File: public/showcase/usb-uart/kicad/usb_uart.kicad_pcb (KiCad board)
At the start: 4 copper layers, 45 x 35.7 mm, 32 parts, among them J1 TYPE-C-31-M-12, J2 UART1, J3 FLOW1, J4 RS485, U1 CH342F, U2 LDO, U3 THVD1450D

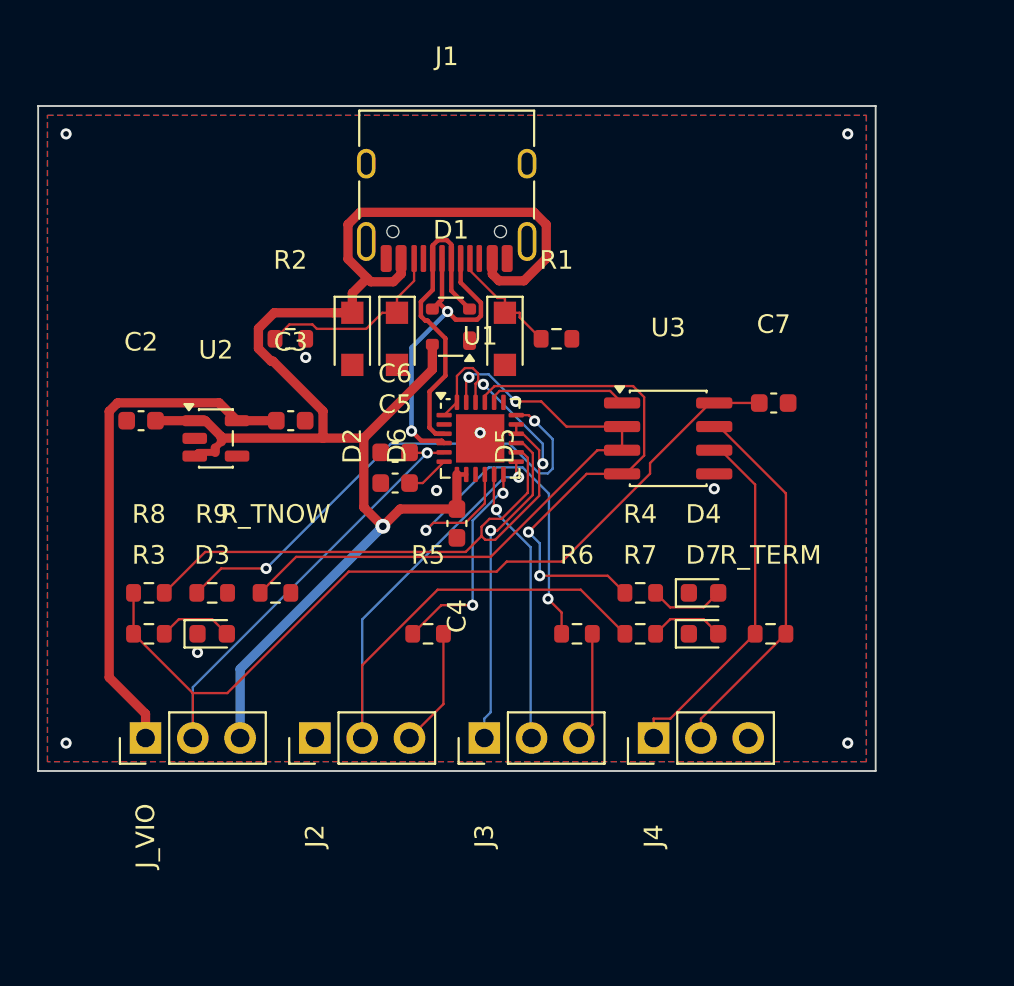
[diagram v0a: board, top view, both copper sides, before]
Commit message: NOISSUE - Update the showcase to board revision B and state its qualification status
Addresses the review on #5: the published route record no longer says fabrication_ready (it is false), the page is labelled an engineering draft with the qualification matrix, gate result and file hashes, every artifact names one revision, and the protection claim says the RS-485 network is not surge-tested.

Signed-off-by: nyagamunene <stevenyaga2014@gmail.com>
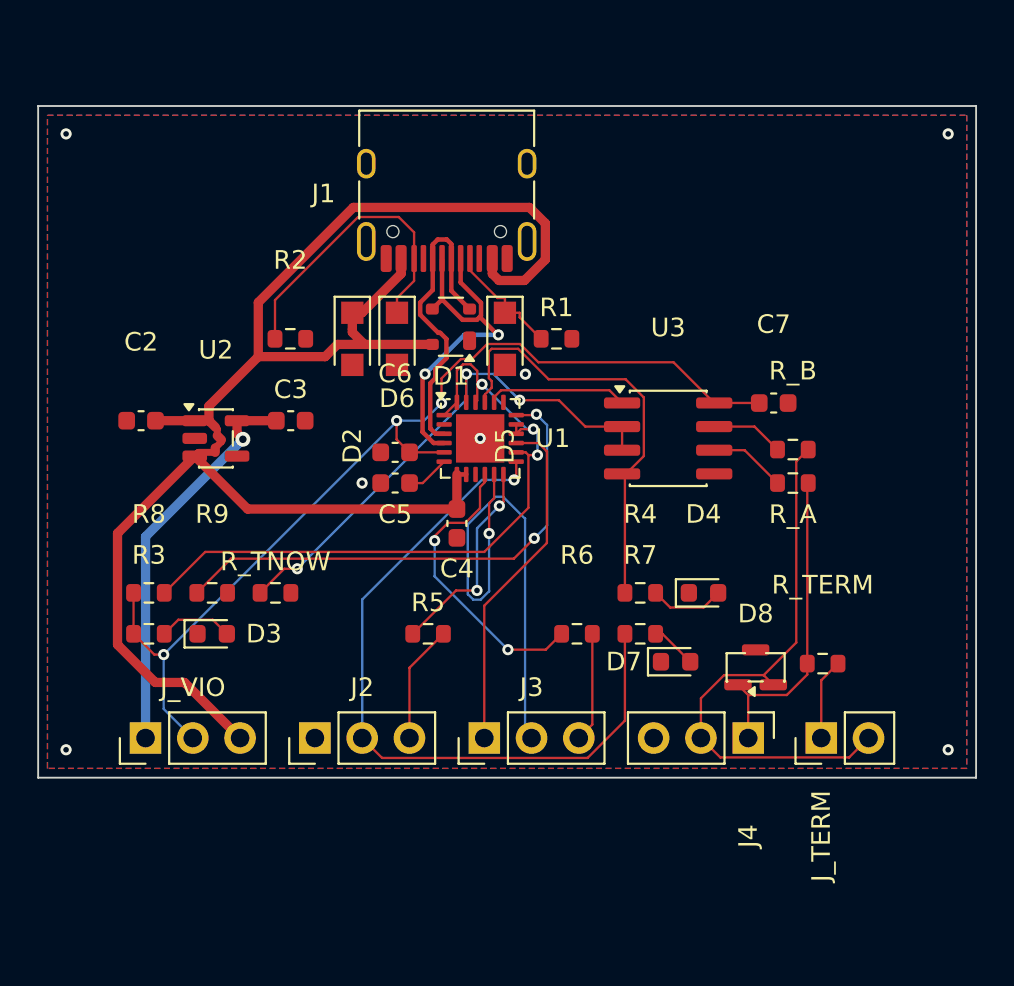
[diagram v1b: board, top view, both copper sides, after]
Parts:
- added D8: TVS, Package_TO_SOT_SMD:SOT-23, F.Cu at (38.6, 29.6)
- added J_TERM: TERM, Connector_PinHeader_2.54mm:PinHeader_1x02_P2.54mm_Vertical, F.Cu at (42.1, 33.4)
- added R_A: 10ohm, Resistor_SMD:R_0603_1608Metric, F.Cu at (40.6, 19.7)
- added R_B: 10ohm, Resistor_SMD:R_0603_1608Metric, F.Cu at (40.6, 17.9)
- moved J4 5.08 mm to (38.2, 33.4), turned to 270 degrees
- moved R_TERM 3.22 mm to (42.2, 29.4)
- moved D7 2.12 mm to (34.3, 29.3)
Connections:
- J4 pad 1: RS485_A -> RS485_A_BUS
- J4 pad 2: RS485_B -> RS485_B_BUS
- R_TERM pad 1: RS485_A -> RS485_A_BUS
- R_TERM pad 2: RS485_B -> RS485_TERM
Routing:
- net RS485_B_BUS: track 0.00 -> 29.7 mm
- net RS485_A_BUS: track 0.00 -> 17.0 mm
- net RS485_B: track 20.4 -> 3.91 mm
- net RS485_A: track 19.4 -> 4.13 mm
- net VIO: track 68.8 -> 54.3 mm, vias 1 -> 3
- net RTS1: track 15.0 -> 27.7 mm
- net MODEM_IDLE: track 45.0 -> 38.3 mm, vias 2 -> 3
- net VBUS: track 85.3 -> 91.8 mm, vias 1 -> 0
- net +3V3: track 27.9 -> 21.5 mm, vias 0 -> 1
- net CC2: track 10.6 -> 16.4 mm
- net CTS1_MCU: track 21.8 -> 15.9 mm
- net TNOW0: track 34.8 -> 29.1 mm, vias 2 -> 3
- net TXD0: track 28.0 -> 23.5 mm, vias 2 -> 0
- net RS485_TERM: track 0.00 -> 4.37 mm
- net LED_TX1: track 4.02 -> 2.48 mm
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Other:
- board size 45 x 35.7 mm -> 50.4 x 36.1 mm

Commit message: NOISSUE - Update the showcase to the Amphenol connector, mounting holes and the re-routed board
The board now uses the Amphenol 12401610E4#2A USB-C connector, which has a 3D model, so the viewer shows the connector. J1 is centred, four M2.5 mounting holes are added, VBUS is routed at 0.3 mm, and the board passes Synth's release gate with 0 DRC errors. Every file, image and number is refreshed from absmach/synth#103 at 3a45fef. Because the routing record now says fabrication_ready, the check requires the page to explain that this is not a manufacturing sign-off.

Signed-off-by: nyagamunene <stevenyaga2014@gmail.com>
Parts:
- added H1: (no value), MountingHole:MountingHole_2.5mm, F.Cu at (2.85, 2.85)
- added H2: (no value), MountingHole:MountingHole_2.5mm, F.Cu at (47.8, 2.85)
- added H3: (no value), MountingHole:MountingHole_2.5mm, F.Cu at (2.85, 24.5)
- added H4: (no value), MountingHole:MountingHole_2.5mm, F.Cu at (47.8, 24.5)
- J1: value TYPE-C-31-M-12 -> 12401610E4#2A; footprint Connector_USB:USB_C_Receptacle_HRO_TYPE-C-31-M-12 -> Connector_USB:USB_C_Receptacle_Amphenol_12401610E4-2A
- moved R2 4.29 mm to (16.9, 14.8)
- moved D2 4.29 mm to (20.2, 14.8)
- moved D5 4.29 mm to (28.4, 14.8)
- moved D6 4.29 mm to (22.6, 14.8)
- moved R1 4.29 mm to (31.1, 14.8)
- moved D1 4.29 mm to (25.5, 14.1)
- moved J1 3.89 mm to (25.2, 5.73)
- moved C4 2.96 mm to (21.6, 24.7)
- moved J2 2.80 mm to (14.9, 36.2)
- moved J3 2.80 mm to (24.0, 36.2)
- moved J4 2.80 mm to (38.2, 36.2)
- moved J_TERM 2.80 mm to (42.1, 36.2)
- moved J_VIO 2.80 mm to (5.82, 36.2)
- moved R_TERM 2.80 mm to (42.2, 32.2)
- moved C5 2.80 mm to (19.2, 22.5)
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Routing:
- net MODEM_IDLE: track 38.3 -> 82.3 mm, vias 3 -> 2
- net RTS1: track 27.7 -> 16.8 mm, vias 1 -> 0
- net VBUS: track 91.8 -> 83.7 mm
- net TXD1: track 39.3 -> 31.7 mm, vias 1 -> 0
- net CTS0_LOW: track 27.6 -> 23.2 mm
- net VIO: track 54.3 -> 58.8 mm, vias 3 -> 1
- net CC2: track 16.4 -> 20.9 mm, vias 0 -> 2
- net USB_DN: track 19.9 -> 15.7 mm
- net CTS1_MCU: track 15.9 -> 12.1 mm, vias 2 -> 0
- net TNOW0: track 29.1 -> 32.5 mm
- net TXD0: track 23.5 -> 20.6 mm
- net USB_DP: track 17.1 -> 19.3 mm, vias 0 -> 3
- net RXD1_MCU: track 11.2 -> 12.2 mm
- net DTR1: track 18.6 -> 18.2 mm, vias 0 -> 1
- net GND: vias 7 -> 6
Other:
- board size 50.4 x 36.1 mm -> 50.4 x 38.3 mm
- net class VBUS_FINE added: clearance 0.127, trace_width 0.3, via_dia 0.6, via_drill 0.3
